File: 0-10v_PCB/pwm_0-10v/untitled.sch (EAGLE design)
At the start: 13 parts, among them U1 OP07CDR, U2 OP07CDR, U3 OP07CDR

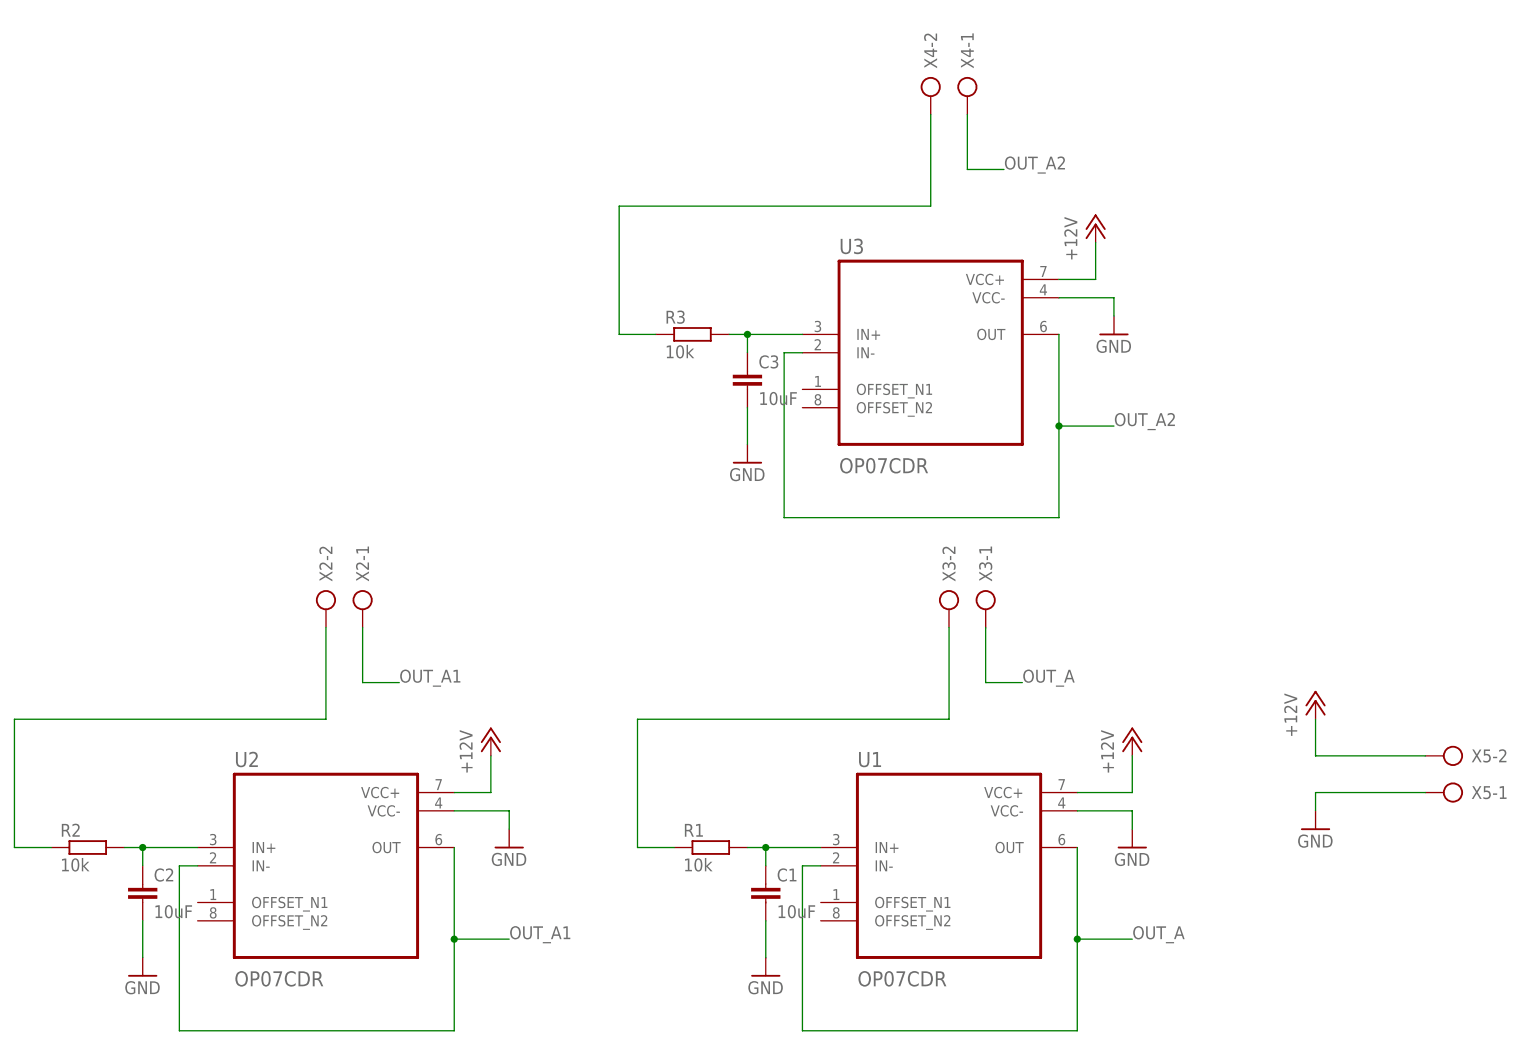
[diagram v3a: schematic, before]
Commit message: added 1.5k pull down resistor to all inputs
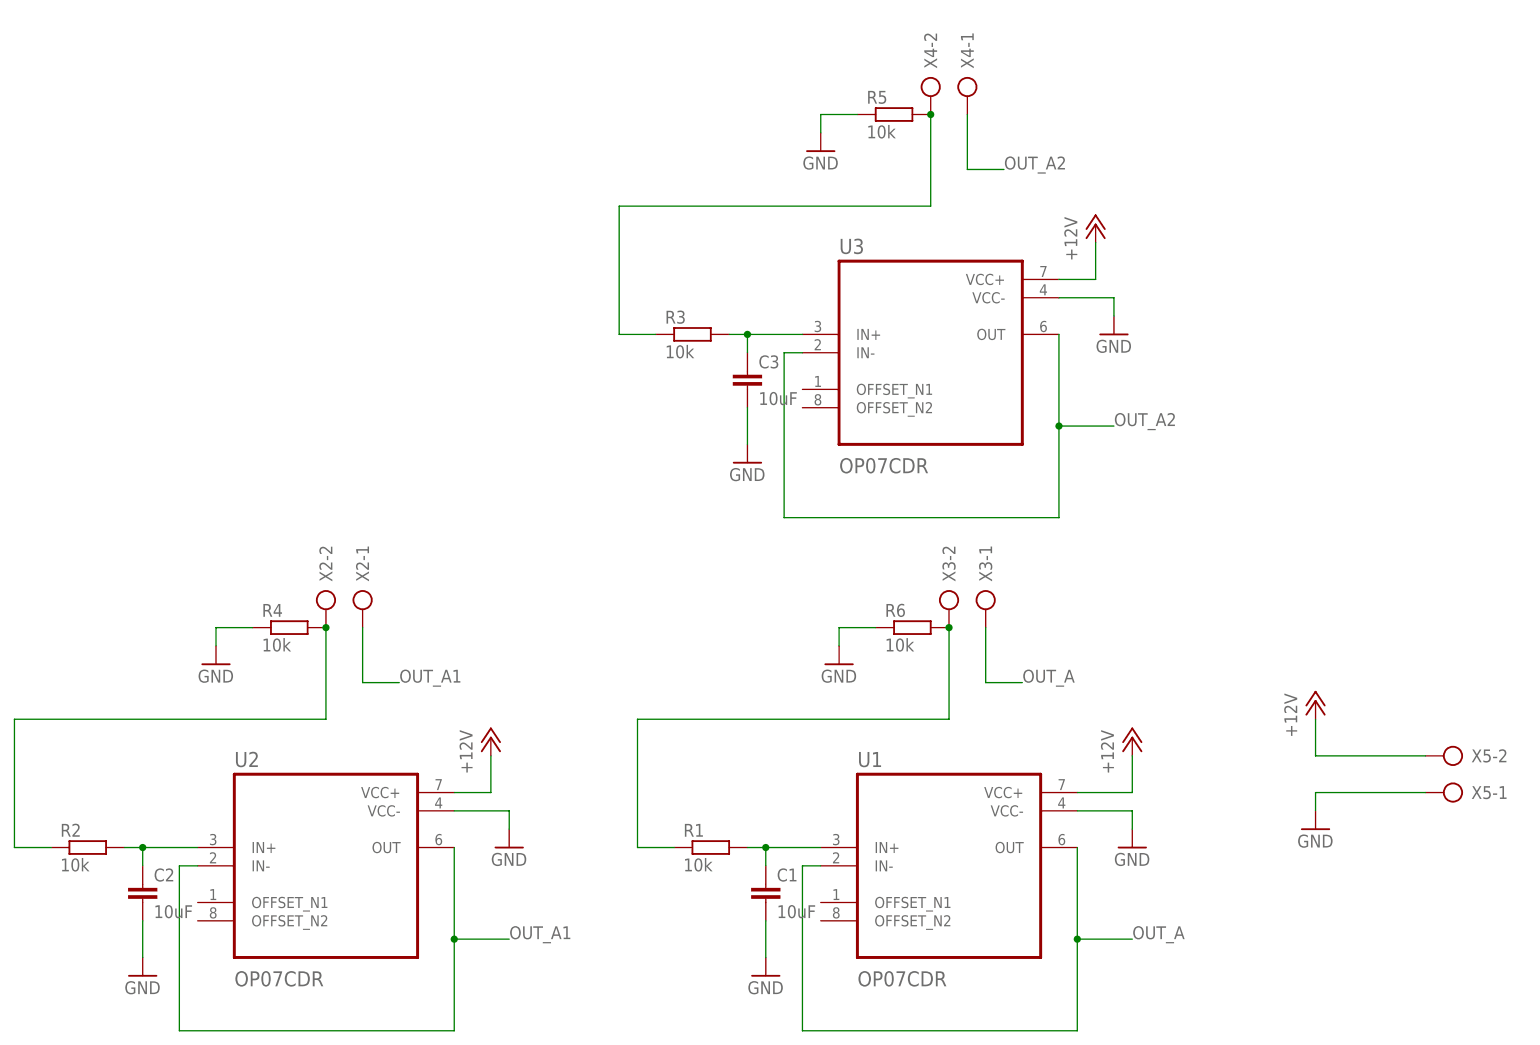
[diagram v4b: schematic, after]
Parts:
- added R4, R5, R6: 10k, rcl:R-EU_M0805
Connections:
- net GND: now also R4.1, R5.1, R6.1
- net N$1: now also R6.2
- net N$3: now also R4.2
- net N$5: now also R5.2
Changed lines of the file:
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@@
 <part name="X4" library="con-ptr500" library_urn="urn:adsk.eagle:library:181" deviceset="AK500/2" device="" package3d_urn="urn:adsk.eagle:package:9880/1"/>
 <part name="X5" library="con-ptr500" library_urn="urn:adsk.eagle:library:181" deviceset="AK500/2" device="" package3d_urn="urn:adsk.eagle:package:9880/1"/>
+<part name="R4" library="rcl" library_urn="urn:adsk.eagle:library:334" deviceset="R-EU_" device="M0805" package3d_urn="urn:adsk.eagle:package:23556/2" value="10k"/>
+<part name="GND9" library="supply1" library_urn="urn:adsk.eagle:library:371" deviceset="GND" device=""/>
+<part name="R5" library="rcl" library_urn="urn:adsk.eagle:library:334" deviceset="R-EU_" device="M0805" package3d_urn="urn:adsk.eagle:package:23556/2" value="10k"/>
+<part name="GND8" library="supply1" library_urn="urn:adsk.eagle:library:371" deviceset="GND" device=""/>
+<part name="R6" library="rcl" library_urn="urn:adsk.eagle:library:334" deviceset="R-EU_" device="M0805" package3d_urn="urn:adsk.eagle:package:23556/2" value="10k"/>
+<part name="GND10" library="supply1" library_urn="urn:adsk.eagle:library:371" deviceset="GND" device=""/>
 </parts>
 <sheets>
@@
 <attribute name="VALUE" x="135.89" y="90.043" size="1.778" layer="96" rot="R180"/>
 </instance>
+<instance part="R4" gate="G$1" x="-30.48" y="104.14" smashed="yes">
+<attribute name="NAME" x="-34.29" y="105.6386" size="1.778" layer="95"/>
+<attribute name="VALUE" x="-34.29" y="100.838" size="1.778" layer="96"/>
+</instance>
+<instance part="GND9" gate="1" x="-40.64" y="99.06" smashed="yes">
+<attribute name="VALUE" x="-43.18" y="96.52" size="1.778" layer="96"/>
+</instance>
+<instance part="R5" gate="G$1" x="53.34" y="175.26" smashed="yes">
+<attribute name="NAME" x="49.53" y="176.7586" size="1.778" layer="95"/>
+<attribute name="VALUE" x="49.53" y="171.958" size="1.778" layer="96"/>
+</instance>
+<instance part="GND8" gate="1" x="43.18" y="170.18" smashed="yes">
+<attribute name="VALUE" x="40.64" y="167.64" size="1.778" layer="96"/>
+</instance>
+<instance part="R6" gate="G$1" x="55.88" y="104.14" smashed="yes">
+<attribute name="NAME" x="52.07" y="105.6386" size="1.778" layer="95"/>
+<attribute name="VALUE" x="52.07" y="100.838" size="1.778" layer="96"/>
+</instance>
+<instance part="GND10" gate="1" x="45.72" y="99.06" smashed="yes">
+<attribute name="VALUE" x="43.18" y="96.52" size="1.778" layer="96"/>
+</instance>
 </instances>
 <busses>
@@
 <pinref part="GND7" gate="1" pin="GND"/>
 <wire x1="33.02" y1="134.62" x2="33.02" y2="129.54" width="0.1524" layer="91"/>
+</segment>
+<segment>
+<pinref part="GND9" gate="1" pin="GND"/>
+<wire x1="-40.64" y1="101.6" x2="-40.64" y2="104.14" width="0.1524" layer="91"/>
+<pinref part="R4" gate="G$1" pin="1"/>
+<wire x1="-40.64" y1="104.14" x2="-35.56" y2="104.14" width="0.1524" layer="91"/>
+</segment>
+<segment>
+<pinref part="GND8" gate="1" pin="GND"/>
+<wire x1="43.18" y1="172.72" x2="43.18" y2="175.26" width="0.1524" layer="91"/>
+<pinref part="R5" gate="G$1" pin="1"/>
+<wire x1="43.18" y1="175.26" x2="48.26" y2="175.26" width="0.1524" layer="91"/>
+</segment>
+<segment>
+<pinref part="GND10" gate="1" pin="GND"/>
+<wire x1="45.72" y1="101.6" x2="45.72" y2="104.14" width="0.1524" layer="91"/>
+<pinref part="R6" gate="G$1" pin="1"/>
+<wire x1="45.72" y1="104.14" x2="50.8" y2="104.14" width="0.1524" layer="91"/>
 </segment>
 </net>
@@
 <wire x1="17.78" y1="73.66" x2="22.86" y2="73.66" width="0.1524" layer="91"/>
 <pinref part="X3" gate="-2" pin="KL"/>
+<pinref part="R6" gate="G$1" pin="2"/>
+<junction x="60.96" y="104.14"/>
 </segment>
 </net>
@@
 <wire x1="-68.58" y1="73.66" x2="-63.5" y2="73.66" width="0.1524" layer="91"/>
 <pinref part="X2" gate="-2" pin="KL"/>
+<pinref part="R4" gate="G$1" pin="2"/>
+<junction x="-25.4" y="104.14"/>
 </segment>
 </net>
@@
 <wire x1="15.24" y1="144.78" x2="20.32" y2="144.78" width="0.1524" layer="91"/>
 <pinref part="X4" gate="-2" pin="KL"/>
-</segment>
-</net>
+<pinref part="R5" gate="G$1" pin="2"/>
+<junction x="58.42" y="175.26"/>
+</segment>
+</net>

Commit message: changed pulldown resistors to 1.5k instead of 10k
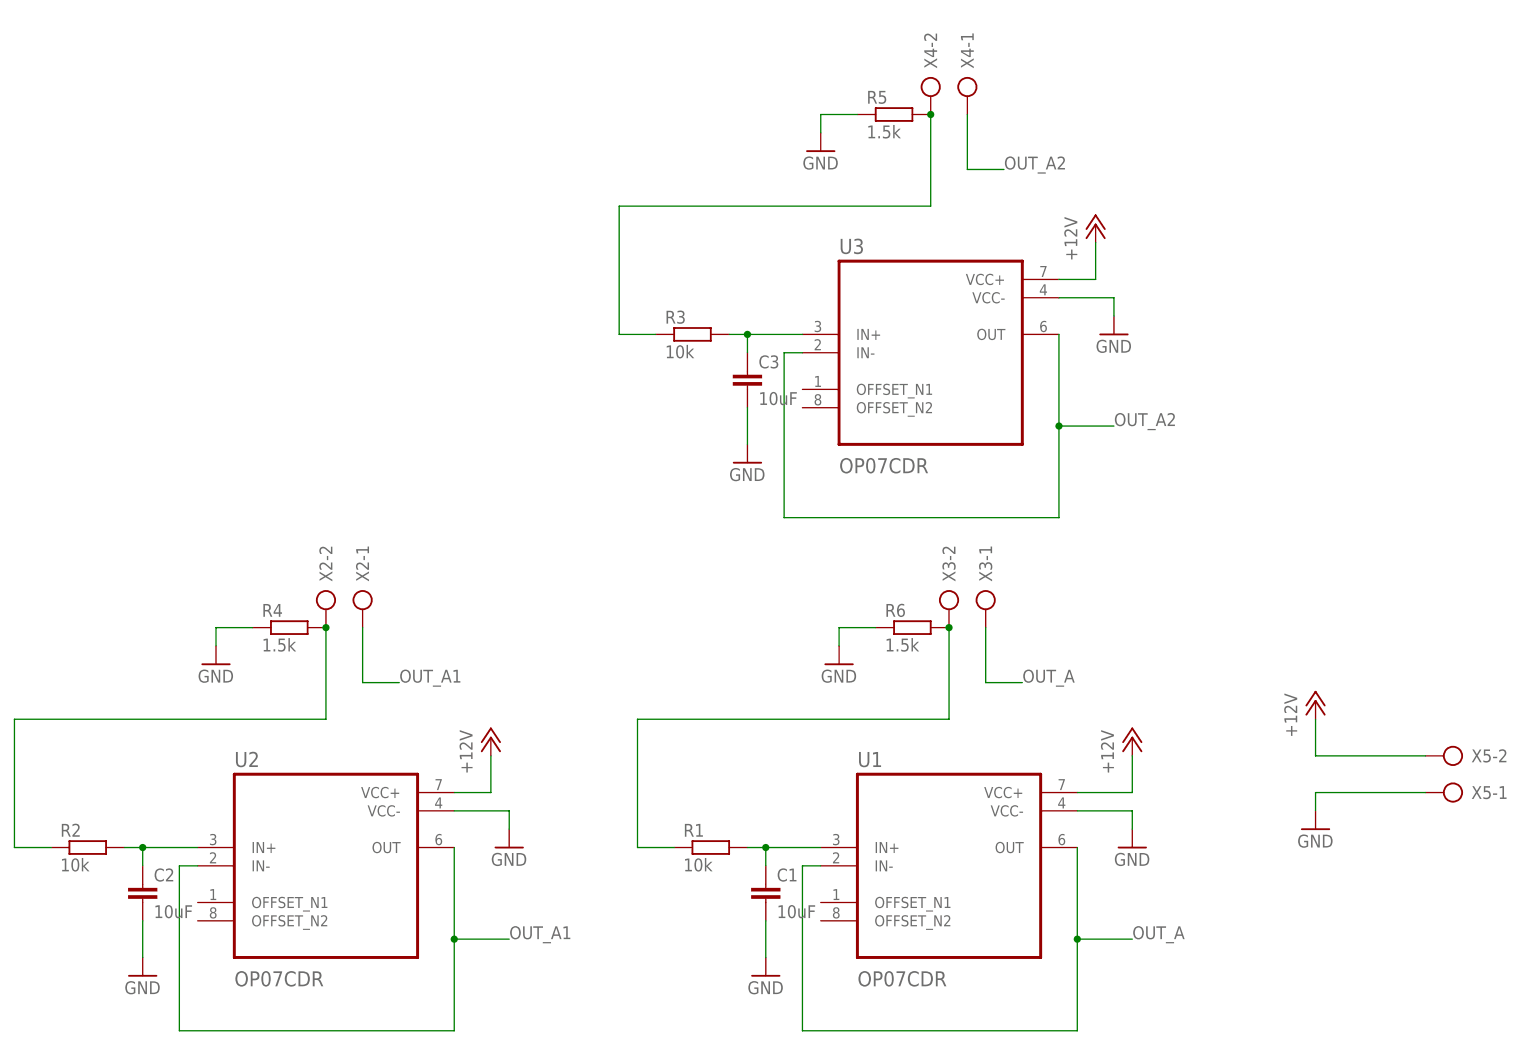
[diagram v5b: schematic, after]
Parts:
- R4, R5, R6: value 10k -> 1.5k
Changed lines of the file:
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@@
 <part name="X4" library="con-ptr500" library_urn="urn:adsk.eagle:library:181" deviceset="AK500/2" device="" package3d_urn="urn:adsk.eagle:package:9880/1"/>
 <part name="X5" library="con-ptr500" library_urn="urn:adsk.eagle:library:181" deviceset="AK500/2" device="" package3d_urn="urn:adsk.eagle:package:9880/1"/>
-<part name="R4" library="rcl" library_urn="urn:adsk.eagle:library:334" deviceset="R-EU_" device="M0805" package3d_urn="urn:adsk.eagle:package:23556/2" value="10k"/>
+<part name="R4" library="rcl" library_urn="urn:adsk.eagle:library:334" deviceset="R-EU_" device="M0805" package3d_urn="urn:adsk.eagle:package:23556/2" value="1.5k"/>
 <part name="GND9" library="supply1" library_urn="urn:adsk.eagle:library:371" deviceset="GND" device=""/>
-<part name="R5" library="rcl" library_urn="urn:adsk.eagle:library:334" deviceset="R-EU_" device="M0805" package3d_urn="urn:adsk.eagle:package:23556/2" value="10k"/>
+<part name="R5" library="rcl" library_urn="urn:adsk.eagle:library:334" deviceset="R-EU_" device="M0805" package3d_urn="urn:adsk.eagle:package:23556/2" value="1.5k"/>
 <part name="GND8" library="supply1" library_urn="urn:adsk.eagle:library:371" deviceset="GND" device=""/>
-<part name="R6" library="rcl" library_urn="urn:adsk.eagle:library:334" deviceset="R-EU_" device="M0805" package3d_urn="urn:adsk.eagle:package:23556/2" value="10k"/>
+<part name="R6" library="rcl" library_urn="urn:adsk.eagle:library:334" deviceset="R-EU_" device="M0805" package3d_urn="urn:adsk.eagle:package:23556/2" value="1.5k"/>
 <part name="GND10" library="supply1" library_urn="urn:adsk.eagle:library:371" deviceset="GND" device=""/>
 </parts>
